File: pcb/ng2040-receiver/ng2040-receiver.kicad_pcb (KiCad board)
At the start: 2 copper layers, 40 x 37 mm, 15 parts, among them J1 DB15_F, U1 RP2040-Zero, U2 NRF24L01_Breakout

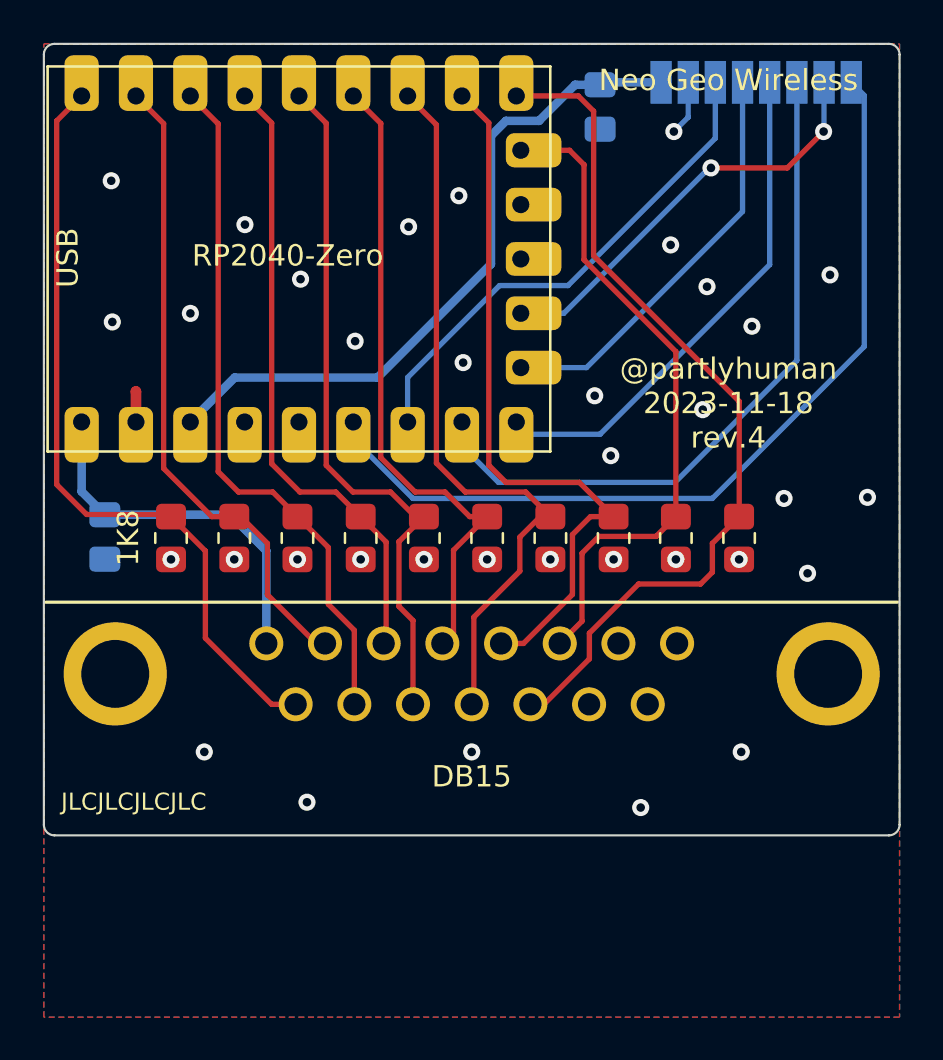
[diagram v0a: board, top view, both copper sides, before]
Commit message: Reworking controller board to put pico on back for LED to shine through
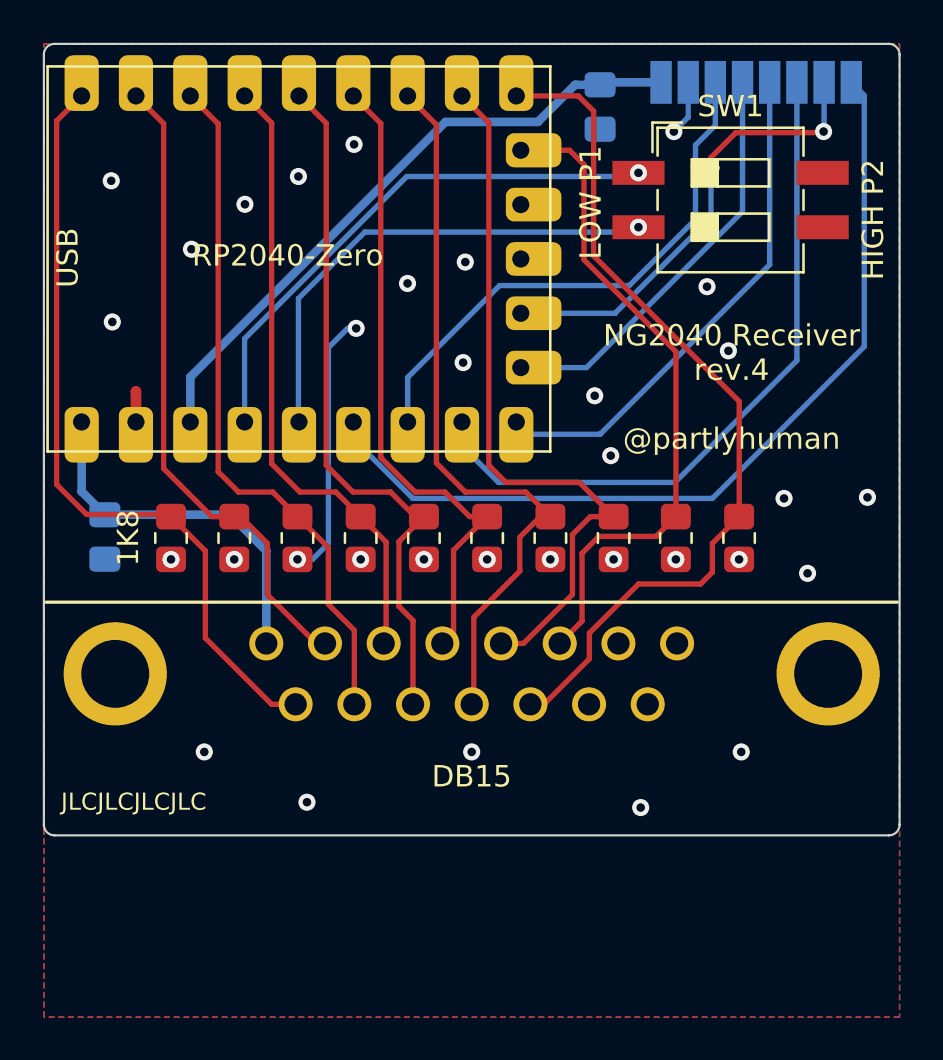
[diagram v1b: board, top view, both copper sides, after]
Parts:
- added SW1: OPTS, Button_Switch_SMD:SW_DIP_SPSTx02_Slide_6.7x6.64mm_W8.61mm_P2.54mm_LowProfile, F.Cu at (112.1, 64.3)
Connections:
- U1 pad 19: unconnected-(U1-GP28-Pad19) -> /SET_POWER
- U1 pad 20: unconnected-(U1-GP29-Pad20) -> /SET_PLAYER
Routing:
- net /SET_PLAYER: track 0.00 -> 25.5 mm, vias 0 -> 1
- net /SET_POWER: track 0.00 -> 23.1 mm, vias 0 -> 1
- net GND: track 4.00 -> 16.6 mm, vias 35 -> 33
- net /3V3: track 32.1 -> 29.8 mm
- net /CE: track 23.7 -> 25.4 mm
- net /MISO: track 20.0 -> 21.6 mm
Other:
- board text added: "${TITLE} rev.${REVISION} ${COMPANY}"
- board text added: "HIGH P2"
- board text added: "LOW P1"
- board text removed: "${COMPANY} ${ISSUE_DATE} rev.${REVISION}"
- board text removed: "Neo Geo Wireless"
